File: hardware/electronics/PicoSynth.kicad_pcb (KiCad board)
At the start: 2 copper layers, 155.1 x 80.9 mm, 126 parts, among them J1 Conn_01x06_Socket, J3 Conn_01x04_Socket, J4 Conn_01x09_Socket, SW1 RotaryEncoder_Switch_MP, SW10 SW_Push_45deg, SW11 SW_Push_45deg, SW12 SW_Push_45deg, SW13 SW_Push_45deg, SW14 SW_Push_45deg, SW15 SW_Push_45deg, SW16 SW_Push_45deg, SW17 SW_Push_45deg, SW18 SW_Push_45deg, SW19 SW_Push_45deg, SW2 RotaryEncoder_Switch_MP, SW20 SW_Push_45deg, SW3 RotaryEncoder_Switch_MP, SW4 RotaryEncoder_Switch_MP, SW5 SW_Push_45deg, SW6 SW_Push_45deg, SW7 SW_Push_45deg, SW8 SW_Push_45deg, SW9 SW_Push_45deg, U1 Pico, U5 PCF8574, U6 PCF8574, U7 PCF8574

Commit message: This layout could work, need to ponder
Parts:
- added C35: 2.2uF, Cern_Ignition:C_0805_2012Metric_Pad1.18x1.45mm_HandSolder_modif, F.Cu at (249.5, 88.8)
- added C36: 100nF, Cern_Ignition:C_0805_2012Metric_Pad1.18x1.45mm_HandSolder_modif, F.Cu at (264.7, 85.7)
- added C37: 10uF, Cern_Ignition:C_1206_3216Metric_Pad1.33x1.80mm_HandSolder_modif, F.Cu at (265.3, 83.5)
- added JP14: A2_Jumper, Jumper:SolderJumper-3_P1.3mm_Open_RoundedPad1.0x1.5mm_NumberLabels, F.Cu at (266.9, 91.6)
- added U8: AMS1117-3.3, Package_TO_SOT_SMD:SOT-223-3_TabPin2, F.Cu at (256.7, 86.1)
- C15, C16, D18, D19, D20, D21, D22, D23, D24, D25, D26, D27, D28, D29, D30, D31, D32, D33, J3, R23, R24, R25, R26, R27, R28, R29, R30, R33, R34, R35, R36, R37, R38, R39, R40, R7, R8, SW1, SW2, SW3, SW4, U5: moved to F.Cu
- C29, C30, C31, C32, D10, D11, D12, D13, D14, D15, D16, D17, D2, D3, D4, D5, D6, D7, D8, D9, JP10, JP11, JP12, JP13, JP5, JP6, JP7, JP8, JP9, R10, R11, R12, R13, R14, R15, R16, R17, R18, R19, R20, R21, R22, R31, R32, R9, U1, U6, U7: moved to B.Cu
- SW10, SW11, SW12, SW13, SW14, SW15, SW16, SW17, SW18, SW19, SW20, SW5, SW6, SW7, SW8, SW9: footprint Cherry_MX_switches:Cherry-MX_PCB-Mounted_LTST-A683CEGBW_Kailh_Socket -> Cherry_MX_switches:Cherry-MX_PCB-Mounted_LTST-A683CEGBW_Kailh_Socket_modif; moved to F.Cu
- moved D16 198.9 mm to (238.4, 106.6)
- moved D17 196.2 mm to (235.7, 124.0)
- moved D33 184.3 mm to (229.6, 142.0), turned to 180 degrees
- moved SW20 184.3 mm to (229.7, 132.3), turned to 0 degrees
- moved SW19 184.2 mm to (229.6, 113.4), turned to 0 degrees
- moved D29 184.2 mm to (229.6, 122.8), turned to 180 degrees
- moved JP5 180.5 mm to (30.1, 65.5), turned to 180 degrees
- moved JP6 180.5 mm to (30.1, 69.3), turned to 180 degrees
- moved JP7 180.5 mm to (30.1, 73.1), turned to 180 degrees
- moved R36 175.6 mm to (225.3, 122.8), turned to 0 degrees
- moved R40 175.6 mm to (225.3, 142.0), turned to 0 degrees
- moved U5 167.2 mm to (36.8, 72.4), turned to 0 degrees
- moved C29 165.6 mm to (54.7, 89.5), turned to 180 degrees
- moved C30 165.6 mm to (54.7, 92.2), turned to 180 degrees
- moved C31 165.6 mm to (54.7, 95.0), turned to 180 degrees
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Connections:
- J3 pad 2: /+3V3 -> /+5V
- JP11 pad 1: GND -> /+3V3
- JP11 pad 3: /+3V3 -> GND
- U1 pad 1: unconnected-(U1-GPIO0-Pad1)_1 -> /Encoder3_Sw
- U1 pad 10: /Encoder0_B -> /Encoder1_A
- U1 pad 11: /Encoder0_Sw -> /Encoder1_B
- U1 pad 12: /Encoder1_Sw -> /Encoder0_Sw
- U1 pad 14: /Encoder1_A -> /Encoder0_A
- U1 pad 15: /Encoder1_B -> /Encoder0_B
- U1 pad 16: /SDA_Bus_0 -> unconnected-(U1-GPIO12-Pad16)
- U1 pad 17: /SCL_Bus_0 -> unconnected-(U1-GPIO13-Pad17)
- U1 pad 19: /SDA_Bus_1 -> unconnected-(U1-GPIO14-Pad19)
- U1 pad 2: unconnected-(U1-GPIO1-Pad2) -> /Encoder3_A
- U1 pad 20: /SCL_Bus_1 -> unconnected-(U1-GPIO15-Pad20)
- U1 pad 25: /Encoder2_Sw -> unconnected-(U1-GPIO19-Pad25)
- U1 pad 26: /Encoder2_B -> unconnected-(U1-GPIO20-Pad26)
- U1 pad 27: /Encoder2_A -> unconnected-(U1-GPIO21-Pad27)
- U1 pad 29: /Encoder3_Sw -> unconnected-(U1-GPIO22-Pad29)
- U1 pad 30: /Encoder3_B -> unconnected-(U1-RUN-Pad30)
- U1 pad 31: /Encoder3_A -> unconnected-(U1-GPIO26_ADC0-Pad31)
- U1 pad 36: /+3V3 -> /+3V3_Pico
- U1 pad 4: /CLK -> /Encoder3_B
- U1 pad 5: /CMD -> /Encoder2_Sw
- U1 pad 6: /DAT0 -> /Encoder2_A
- U1 pad 7: /CD -> /Encoder2_B
- U1 pad 9: /Encoder0_A -> /Encoder1_Sw
- U5 pad 13: unconnected-(U5-~{INT}-Pad13) -> /Switch_Interrupt
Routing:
- net /+5V: track 0.00 -> 358.6 mm
- net /Pin5: track 0.00 -> 71.3 mm, vias 0 -> 4
- net /Pin7: track 0.00 -> 70.8 mm, vias 0 -> 4
- net /Pin6: track 0.00 -> 63.2 mm, vias 0 -> 4
- net /Pin4: track 0.00 -> 62.7 mm, vias 0 -> 4
- net /Pin3: track 0.00 -> 38.1 mm
- net /Pin2: track 0.36 -> 38.5 mm
- net /Pin0: track 0.00 -> 38.1 mm
- net /Pin1: track 0.00 -> 38.0 mm
- net Net-(D10-A): track 0.00 -> 3.03 mm
- net Net-(D16-A): track 0.00 -> 3.03 mm
- net Net-(D12-A): track 0.00 -> 3.03 mm
- net Net-(D5-A): track 0.00 -> 2.93 mm
- net Net-(D4-A): track 0.00 -> 2.90 mm
- net Net-(D14-A): track 0.00 -> 2.90 mm
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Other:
- board size 155.1 x 80.9 mm -> 156.1 x 74.4 mm

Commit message: Basic routing almost complete: 6 more traces to go
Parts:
- removed C33: 2.2uF, Cern_Ignition:C_0805_2012Metric_Pad1.18x1.45mm_HandSolder_modif
- removed C34: 100nF, Cern_Ignition:C_0805_2012Metric_Pad1.18x1.45mm_HandSolder_modif
- removed R41, R42, R43, R44: 10k, Cern_Ignition:R_0805_2012Metric_Pad1.20x1.40mm_HandSolder_modif
- added H1: MountingHole_Pad, MountingHole:MountingHole_2.2mm_M2_Pad_Via, F.Cu at (46.7, 112.5)
- added H2: MountingHole_Pad, MountingHole:MountingHole_2.2mm_M2_Pad_Via, F.Cu at (204.9, 112.4)
- added H3: MountingHole_Pad, MountingHole:MountingHole_2.2mm_M2_Pad_Via, F.Cu at (92.2, 36.0)
- added H4: MountingHole_Pad, MountingHole:MountingHole_2.2mm_M2_Pad_Via, F.Cu at (204.9, 36.0)
- added J5: Line_Out, Connector_PinHeader_2.54mm:PinHeader_1x04_P2.54mm_Vertical, F.Cu at (124.2, 44.8)
- added J6: Conn_01x06_Socket, Connector_PinSocket_2.54mm:PinSocket_1x06_P2.54mm_Vertical, B.Cu at (99.1, 62.0)
- added R45: 10k, Cern_Ignition:R_0805_2012Metric_Pad1.20x1.40mm_HandSolder_modif, F.Cu at (55.9, 56.5)
- added R46: 10k, Cern_Ignition:R_0805_2012Metric_Pad1.20x1.40mm_HandSolder_modif, F.Cu at (69.6, 56.5)
- added R47: 10k, Cern_Ignition:R_0805_2012Metric_Pad1.20x1.40mm_HandSolder_modif, F.Cu at (78.9, 56.5)
- added R48: 10k, Cern_Ignition:R_0805_2012Metric_Pad1.20x1.40mm_HandSolder_modif, F.Cu at (81.2, 56.5)
- added R49: 10k, Cern_Ignition:R_0805_2012Metric_Pad1.20x1.40mm_HandSolder_modif, F.Cu at (65.0, 56.5)
- added R50: 10k, Cern_Ignition:R_0805_2012Metric_Pad1.20x1.40mm_HandSolder_modif, F.Cu at (67.3, 56.5)
- added R51: 10k, Cern_Ignition:R_0805_2012Metric_Pad1.20x1.40mm_HandSolder_modif, F.Cu at (71.9, 56.5)
- added R52: 10k, Cern_Ignition:R_0805_2012Metric_Pad1.20x1.40mm_HandSolder_modif, F.Cu at (74.2, 56.5)
- added R53: 10k, Cern_Ignition:R_0805_2012Metric_Pad1.20x1.40mm_HandSolder_modif, F.Cu at (60.5, 56.5)
- added R54: 10k, Cern_Ignition:R_0805_2012Metric_Pad1.20x1.40mm_HandSolder_modif, F.Cu at (58.2, 56.5)
- C17, C18, C19, C20, C21, C22, C23, C24, C25, C26, C27, C28, JP14, R7, R8: moved to B.Cu
- C29, C30, C31, C32, R21, R22, U6, U7: moved to F.Cu
- R31, R32: value 4.7k -> 10k; moved to F.Cu
- U1: footprint Pi_Pico:RPi_Pico_SMD_TH -> Pi_Pico:RPi_Pico_SMD_TH_No_Debug
- moved C37 210.5 mm to (55.4, 68.6), turned to 90 degrees
- moved JP14 210.3 mm to (57.7, 70.4), turned to 90 degrees
- moved C36 208.7 mm to (56.4, 73.4)
- moved U8 207.0 mm to (50.3, 70.2), turned to -90 degrees
- moved C28 202.5 mm to (45.7, 39.3)
- moved C35 201.9 mm to (49.0, 64.8)
- moved C25 197.7 mm to (48.3, 39.3)
- moved C26 187.9 mm to (53.3, 39.3)
- moved C22 183.1 mm to (55.9, 39.3)
- moved C20 178.3 mm to (58.4, 39.3)
- moved C21 173.7 mm to (60.8, 39.3)
- moved C27 163.9 mm to (66.0, 39.3)
- moved C23 159.2 mm to (68.6, 39.3)
- moved C24 154.4 mm to (71.1, 39.4)
- moved U1 150.9 mm to (69.8, 53.1), turned to -90 degrees
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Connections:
- D11 pad 1: /Pin7 -> /Pin4
- D13 pad 1: /Pin7 -> /Pin4
- D15 pad 1: /Pin7 -> /Pin4
- D17 pad 1: /Pin7 -> /Pin4
- D2 pad 1: /Pin4 -> /Pin0
- D3 pad 1: /Pin4 -> /Pin0
- D4 pad 1: /Pin4 -> /Pin0
- D5 pad 1: /Pin4 -> /Pin0
- D6 pad 1: /Pin5 -> /Pin1
- D7 pad 1: /Pin5 -> /Pin1
- D8 pad 1: /Pin5 -> /Pin1
- D9 pad 1: /Pin5 -> /Pin1
- J3 pad 3: /SCL_Bus_0 -> /SCL_Bus_1
- J3 pad 4: /SDA_Bus_0 -> /SDA_Bus_1
- J4 pad 2: /G -> /G_L
- J4 pad 4: /G -> /G_R
- R21 pad 2: /SDA_Bus_0 -> /SDA_Bus_1
- R22 pad 2: /SCL_Bus_0 -> /SCL_Bus_1
- R31 pad 1: /+3V3 -> /Encoder0_Sw
- R31 pad 2: /SDA_Bus_0 -> /+3V3_Pico
- R32 pad 1: /+3V3 -> /Encoder2_Sw
- R32 pad 2: /SCL_Bus_0 -> /+3V3_Pico
- R7 pad 2: /SCL_Bus_1 -> /SCL_Bus_0
- R8 pad 2: /SDA_Bus_1 -> /SDA_Bus_0
- SW10 pad 1: /Pin1 -> /Pin3
- SW11 pad 1: /Pin2 -> /Pin5
- SW12 pad 1: /Pin3 -> /Pin7
- SW13 pad 1: /Pin0 -> /Pin2
- SW14 pad 1: /Pin0 -> /Pin2
- SW15 pad 1: /Pin1 -> /Pin3
- SW16 pad 1: /Pin1 -> /Pin3
- SW17 pad 1: /Pin2 -> /Pin5
- SW18 pad 1: /Pin2 -> /Pin5
- SW19 pad 1: /Pin3 -> /Pin7
- SW20 pad 1: /Pin3 -> /Pin7
- SW5 pad 1: /Pin0 -> /Pin2
- SW6 pad 1: /Pin1 -> /Pin3
- SW7 pad 1: /Pin2 -> /Pin5
- SW8 pad 1: /Pin3 -> /Pin7
- SW9 pad 1: /Pin0 -> /Pin2
- U1 pad 16: unconnected-(U1-GPIO12-Pad16) -> /BCK
- U1 pad 17: unconnected-(U1-GPIO13-Pad17) -> /LRCK
- U1 pad 19: unconnected-(U1-GPIO14-Pad19) -> /DIN
- U1 pad 21: /BCK -> /SDA_Bus_0
- U1 pad 22: /LRCK -> /SCL_Bus_0
- U1 pad 24: /DIN -> unconnected-(U1-GPIO18-Pad24)
- U1 pad 31: unconnected-(U1-GPIO26_ADC0-Pad31) -> /SDA_Bus_1
- U1 pad 32: unconnected-(U1-GPIO27_ADC1-Pad32)_1 -> /SCL_Bus_1
- U5 pad 14: /SCL_Bus_1 -> /SCL_Bus_0
- U5 pad 15: /SDA_Bus_1 -> /SDA_Bus_0
- U6 pad 14: /SCL_Bus_0 -> /SCL_Bus_1
- U6 pad 15: /SDA_Bus_0 -> /SDA_Bus_1
- U7 pad 14: /SCL_Bus_0 -> /SCL_Bus_1
- U7 pad 15: /SDA_Bus_0 -> /SDA_Bus_1
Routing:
- net /+3V3: track 0.00 -> 173.0 mm, vias 0 -> 11
- net /Encoder3_Sw: track 0.00 -> 170.7 mm, vias 0 -> 1
- net /Encoder3_A: track 0.00 -> 162.8 mm, vias 0 -> 3
- net /Encoder3_B: track 0.00 -> 149.8 mm, vias 0 -> 3
- net /Encoder2_Sw: track 0.00 -> 142.2 mm, vias 0 -> 3
- net /Encoder2_A: track 0.00 -> 134.7 mm, vias 0 -> 3
- net /Encoder2_B: track 0.00 -> 123.2 mm, vias 0 -> 3
- net /+5V: track 358.6 -> 480.9 mm, vias 0 -> 2
- net /Encoder1_Sw: track 0.00 -> 114.2 mm, vias 0 -> 3
- net /Encoder1_A: track 0.00 -> 106.7 mm, vias 0 -> 3
- net /Pin3: track 38.1 -> 143.4 mm, vias 0 -> 3
- net /Pin7: track 70.8 -> 167.3 mm, vias 4 -> 3
- net /Encoder1_B: track 0.00 -> 95.0 mm, vias 0 -> 3
- net /LED_Pin0: track 0.00 -> 93.9 mm, vias 0 -> 2
- net /Pin2: track 38.5 -> 130.2 mm, vias 0 -> 3
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- added copper zone on B.Cu, net GND
- added copper zone on F.Cu, net GND
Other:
- board size 156.1 x 74.4 mm -> 164 x 82.4 mm

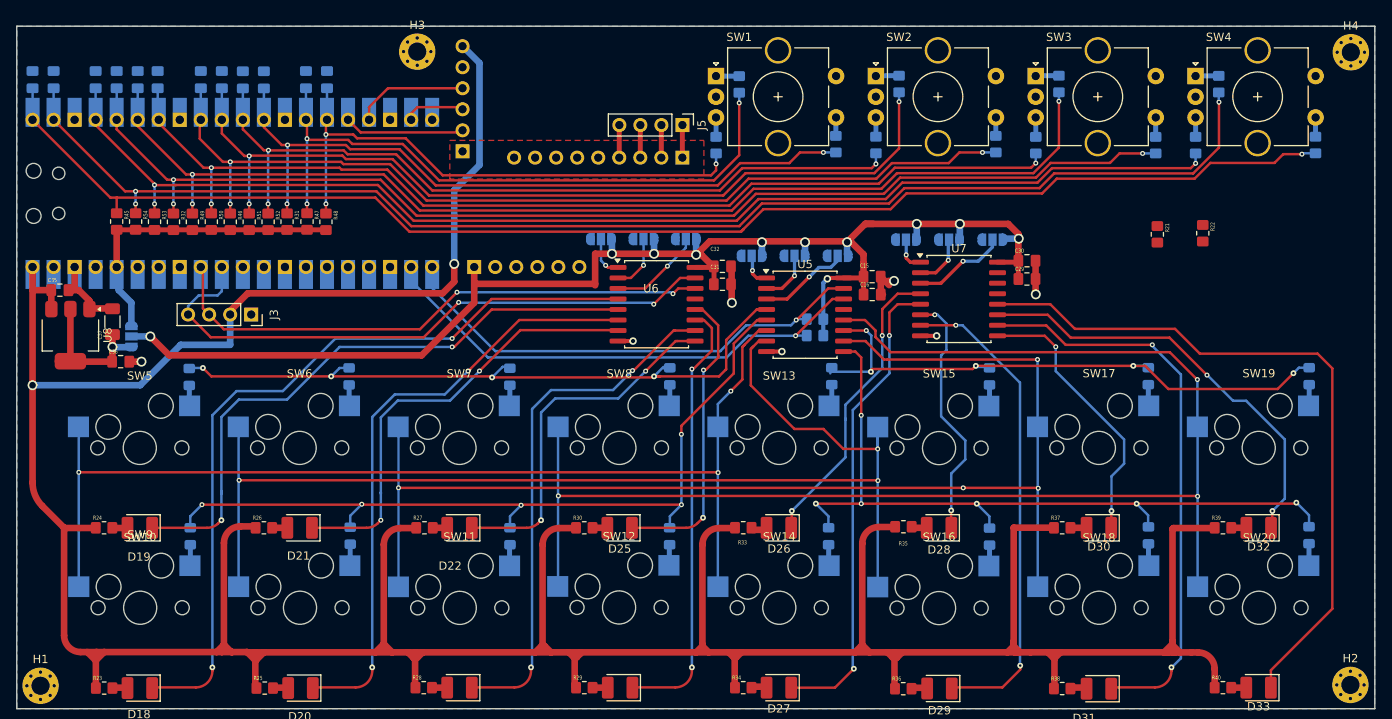
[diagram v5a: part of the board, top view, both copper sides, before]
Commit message: Routing Done, to-do: verify schematic and fix silkscreen
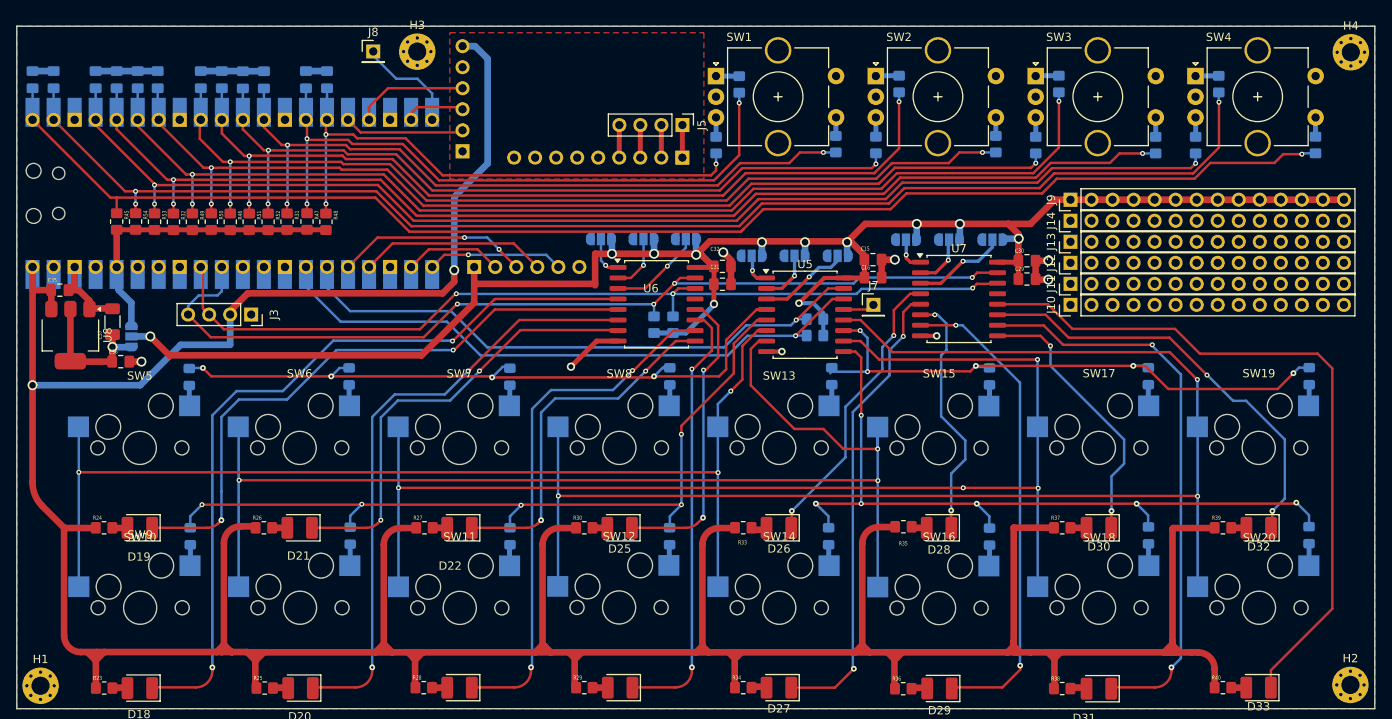
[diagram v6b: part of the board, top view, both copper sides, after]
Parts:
- added J10: Conn_01x14_Socket, Connector_PinHeader_2.54mm:PinHeader_1x14_P2.54mm_Vertical, F.Cu at (171.1, 66.5)
- added J11: Conn_01x14_Socket, Connector_PinHeader_2.54mm:PinHeader_1x14_P2.54mm_Vertical, F.Cu at (171.1, 64.0)
- added J12: Conn_01x14_Socket, Connector_PinHeader_2.54mm:PinHeader_1x14_P2.54mm_Vertical, F.Cu at (171.1, 61.5)
- added J13: Conn_01x14_Socket, Connector_PinHeader_2.54mm:PinHeader_1x14_P2.54mm_Vertical, F.Cu at (171.1, 58.9)
- added J14: Conn_01x14_Socket, Connector_PinHeader_2.54mm:PinHeader_1x14_P2.54mm_Vertical, F.Cu at (171.1, 56.4)
- added J7: Conn_01x01_Socket, Connector_PinHeader_2.54mm:PinHeader_1x01_P2.54mm_Vertical, F.Cu at (147.3, 66.5)
- added J8: Conn_01x01_Socket, Connector_PinHeader_2.54mm:PinHeader_1x01_P2.54mm_Vertical, F.Cu at (86.9, 35.9)
- added J9: Conn_01x14_Socket, Connector_PinHeader_2.54mm:PinHeader_1x14_P2.54mm_Vertical, F.Cu at (171.1, 53.8)
- R21, R22: moved to B.Cu
- moved R22 64.9 mm to (123.1, 68.9), turned to 90 degrees
- moved R21 61.8 mm to (120.8, 68.9), turned to 90 degrees
- moved C15 2.06 mm to (147.2, 61.1)
- moved C16 2.06 mm to (147.2, 63.2)
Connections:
- U1 pad 20: unconnected-(U1-GPIO15-Pad20) -> /Switch_Interrupt
- U1 pad 21: /SDA_Bus_0 -> /MISO
- U1 pad 22: /SCL_Bus_0 -> /CS
- U1 pad 24: unconnected-(U1-GPIO18-Pad24) -> /CLK
- U1 pad 25: unconnected-(U1-GPIO19-Pad25) -> /MOSI
- U1 pad 26: unconnected-(U1-GPIO20-Pad26) -> /SDA_Bus_0
- U1 pad 27: unconnected-(U1-GPIO21-Pad27) -> /SCL_Bus_0
- U5 pad 13: /Switch_Interrupt -> Net-(J7-Pin_1)
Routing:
- net /+3V3: track 173.0 -> 225.8 mm, vias 11 -> 12
- net /SCL_Bus_1: track 67.7 -> 110.1 mm, vias 2 -> 3
- net /SDA_Bus_1: track 74.2 -> 115.1 mm, vias 2 -> 4
- net GND: track 29.6 -> 55.2 mm, vias 7 -> 8
- net /MOSI: track 0.00 -> 23.3 mm, vias 0 -> 2
- net /CLK: track 0.00 -> 22.7 mm
- net /MISO: track 0.00 -> 19.0 mm, vias 0 -> 1
- net /CS: track 0.00 -> 13.6 mm
- net /SCL_Bus_0: track 62.0 -> 74.9 mm
- net /Switch_Interrupt: track 0.00 -> 12.7 mm
- net /SDA_Bus_0: track 59.8 -> 72.1 mm
- net Net-(J7-Pin_1): track 0.00 -> 3.99 mm
- net /+5V: track 480.9 -> 482.6 mm
- net /LED_Pin8: track 36.5 -> 35.5 mm
- net /LED_Pin9: track 57.6 -> 56.6 mm
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
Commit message: TO-DO: fix silkscreen
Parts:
- added JP15: SolderJumper_2_Open, Jumper:SolderJumper-2_P1.3mm_Open_RoundedPad1.0x1.5mm, B.Cu at (188.8, 51.4)
- moved H3 45.5 mm to (46.7, 36.2)
- moved J8 7.13 mm to (94.0, 35.4)
- moved C25 2.54 mm to (50.8, 39.3)
- moved C28 1.38 mm to (46.8, 40.3), turned to 0 degrees
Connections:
- J9 pad 10: /+3V3 -> Net-(J9-Pin_10)
- J9 pad 11: /+3V3 -> Net-(J9-Pin_10)
- J9 pad 12: /+3V3 -> Net-(J9-Pin_10)
- J9 pad 13: /+3V3 -> Net-(J9-Pin_10)
- J9 pad 14: /+3V3 -> Net-(J9-Pin_10)
- J9 pad 8: /+3V3 -> Net-(J9-Pin_10)
- J9 pad 9: /+3V3 -> Net-(J9-Pin_10)
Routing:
- net Net-(J9-Pin_10): track 0.00 -> 18.8 mm
- net /+3V3: track 225.8 -> 211.5 mm
- net /Switch_Interrupt: track 12.7 -> 8.76 mm
- net /LED_Pin15: track 85.3 -> 82.3 mm
- net GND: track 55.2 -> 57.4 mm
- net /Encoder3_A: track 162.8 -> 164.4 mm
- net /LED_Pin10: track 30.4 -> 30.9 mm

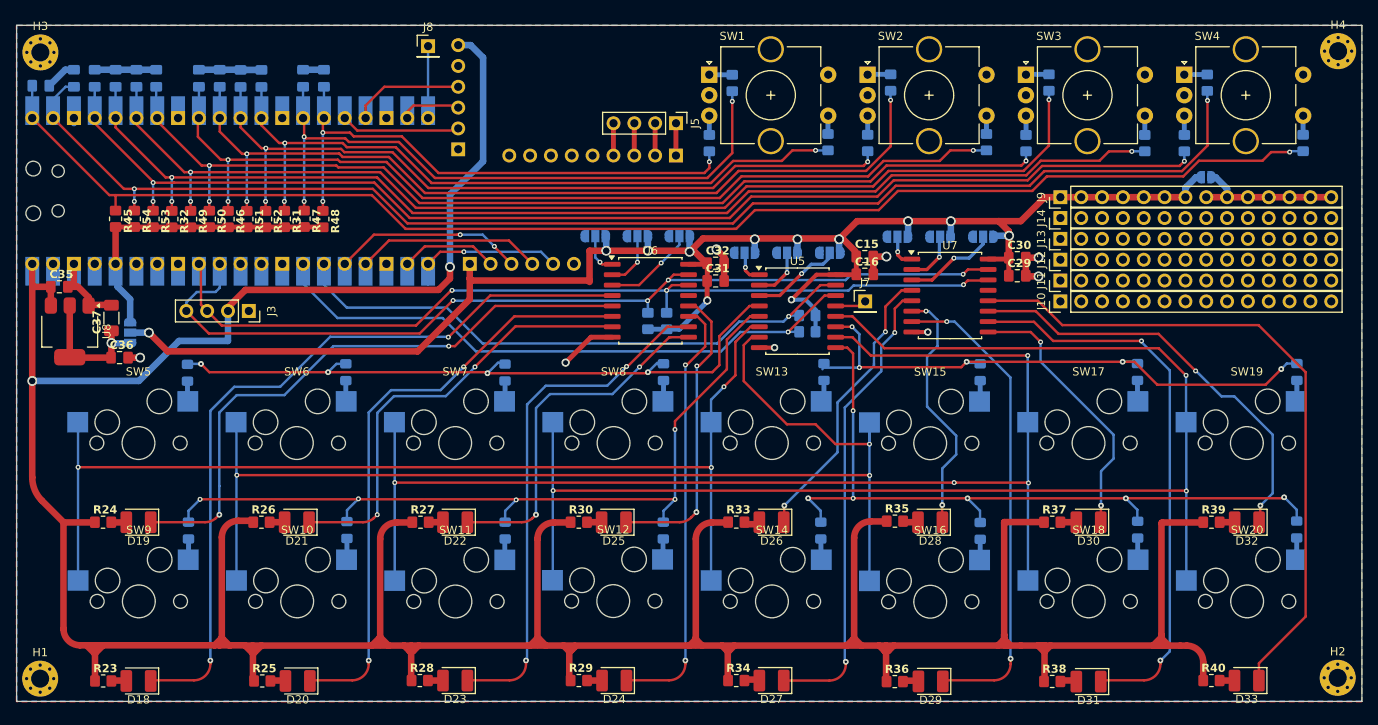
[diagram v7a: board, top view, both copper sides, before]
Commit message: Finished layout, no errors in DRC, silkscreen aso finished
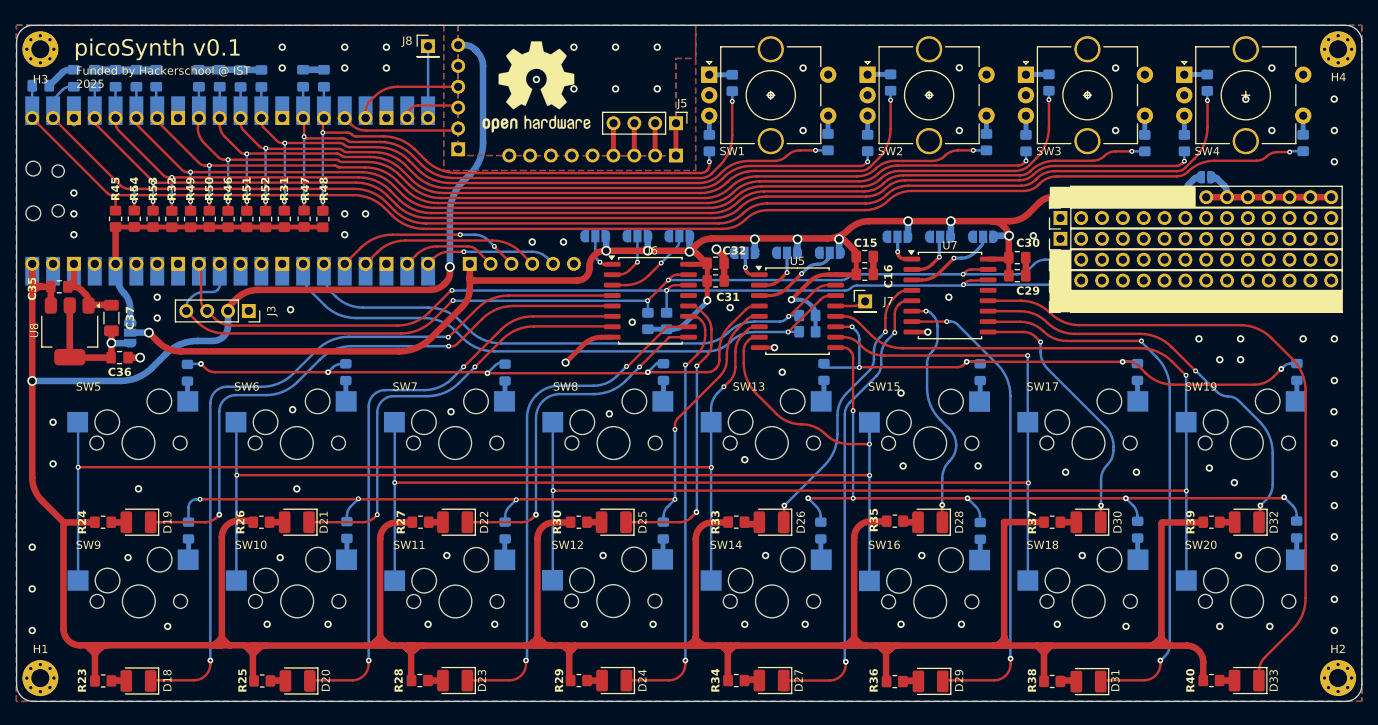
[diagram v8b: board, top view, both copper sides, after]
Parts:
- added REF**: OSHW-Logo2_14.6x12mm_SilkScreen, Symbol:OSHW-Logo2_14.6x12mm_SilkScreen, F.Cu at (107.2, 40.4)
- moved H3 0.38 mm to (46.7, 35.8)
- moved H4 0.23 mm to (204.9, 35.8)
- moved H1 0.08 mm to (46.7, 112.5)
- moved H2 0.05 mm to (204.9, 112.5)
- turned JP11 to 0 degrees
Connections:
- J1 pad 1: GND -> unconnected-(J1-Pin_1-Pad1)
- J11 pad 1: unconnected-(J11-Pin_1-Pad1) -> /SCL_Bus_1
- J12 pad 1: unconnected-(J12-Pin_1-Pad1) -> /SDA_Bus_1
- JP11 pad 1: /+3V3 -> GND
- JP11 pad 3: GND -> /+3V3
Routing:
- net /+5V: track 482.6 -> 501.8 mm
- net /SDA_Bus_1: track 115.1 -> 126.1 mm
- net /SCL_Bus_1: track 110.1 -> 119.0 mm
- net GND: track 57.4 -> 50.7 mm, vias 8 -> 105
- net /Encoder3_A: track 164.4 -> 160.6 mm
- net /+3V3: track 211.5 -> 208.1 mm
- net /SCL_Bus_0: track 74.9 -> 71.7 mm
- net /Pin5: track 149.1 -> 146.0 mm, vias 4 -> 3
- net /Pin0: track 83.9 -> 80.8 mm
- net /MISO: track 19.0 -> 16.2 mm
- net /SDA_Bus_0: track 72.1 -> 69.4 mm
- net /Encoder2_Sw: track 142.2 -> 139.5 mm
- net /LED_Pin15: track 82.3 -> 79.8 mm
- net /Encoder2_B: track 123.2 -> 120.9 mm
- net /Encoder2_A: track 134.7 -> 132.5 mm
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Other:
- outline, holes or cut-outs redrawn
- board text added: "+3V3"
- board text added: "Funded by Hackerschool @ IST 2025"
- board text added: "GND"
- board text added: "SCL"
- board text added: "SDA"
- board text added: "picoSynth v0.1"
